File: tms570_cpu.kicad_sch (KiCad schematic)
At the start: 54 parts, among them J12 TSW-103-08-F-S-RA, J3 FTSH-105-01-L-DV-K, U2 TMS570LS0914APGEQQ1

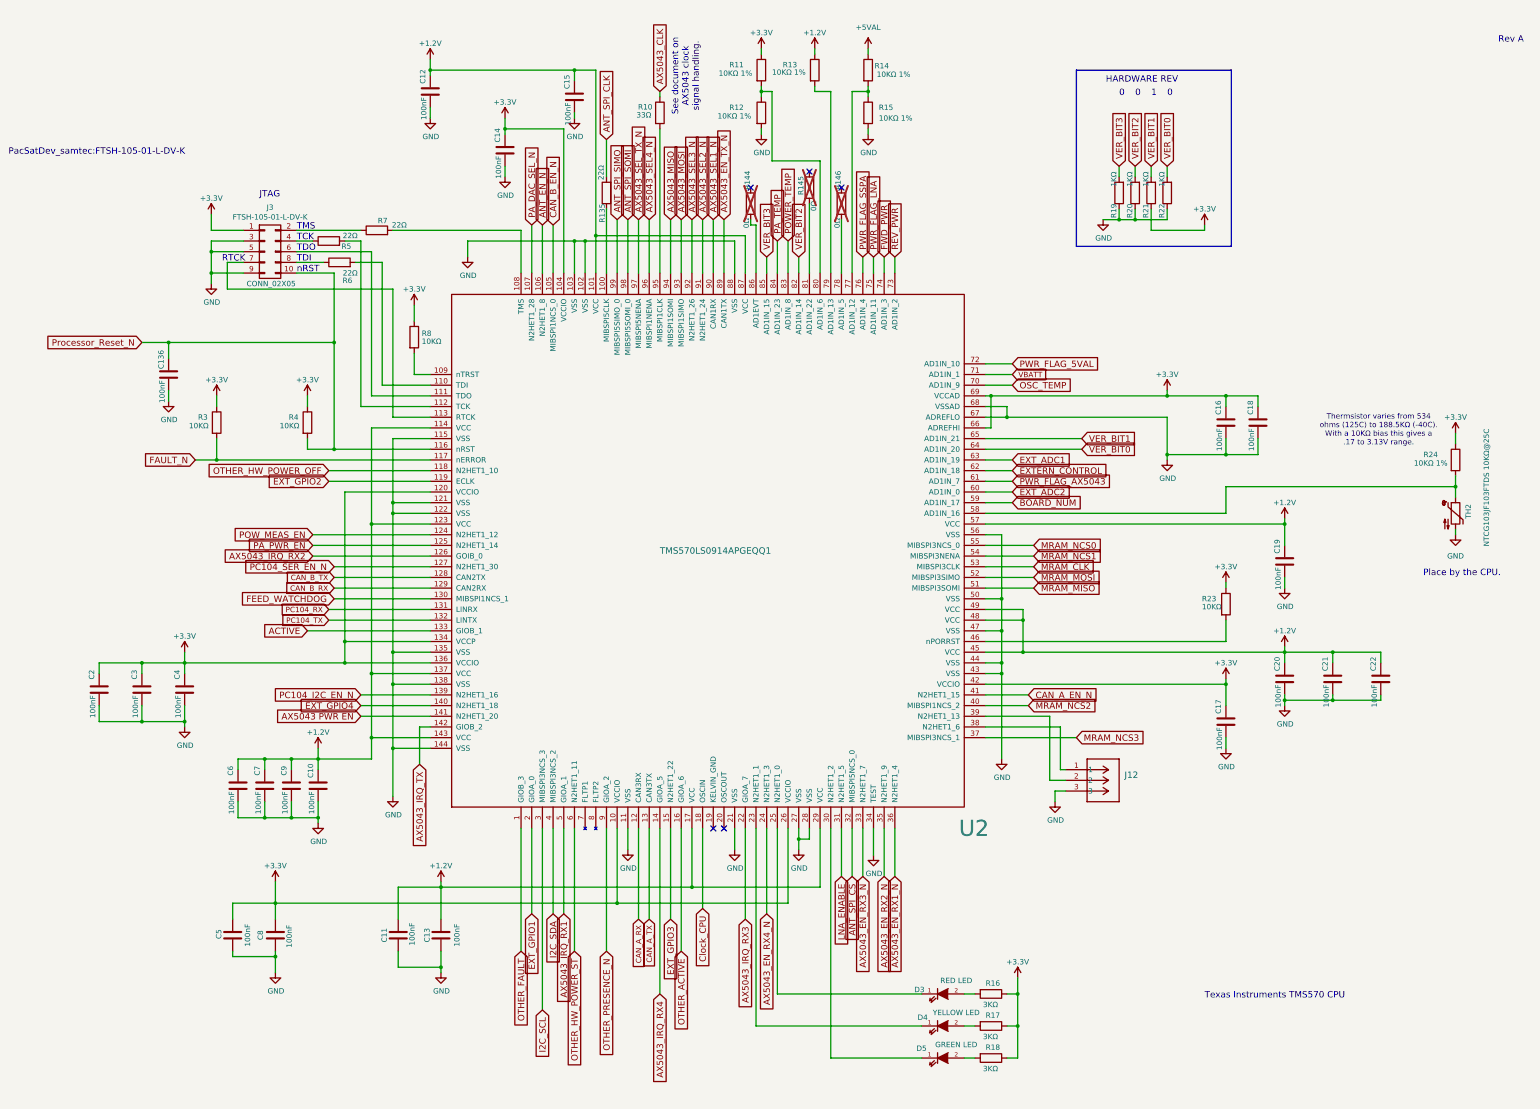
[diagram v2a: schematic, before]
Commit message: Add an interrupt line from the antenna controller to the main CPU
This required moving OTHER\_PRESENCE\_N from GIOA[2] to AD1EVT to free
up a pin with interrupts and using GIOA[2] for ANT\_IRQ\_N.

Signed-off-by: Corey Minyard <corey@minyard.net>
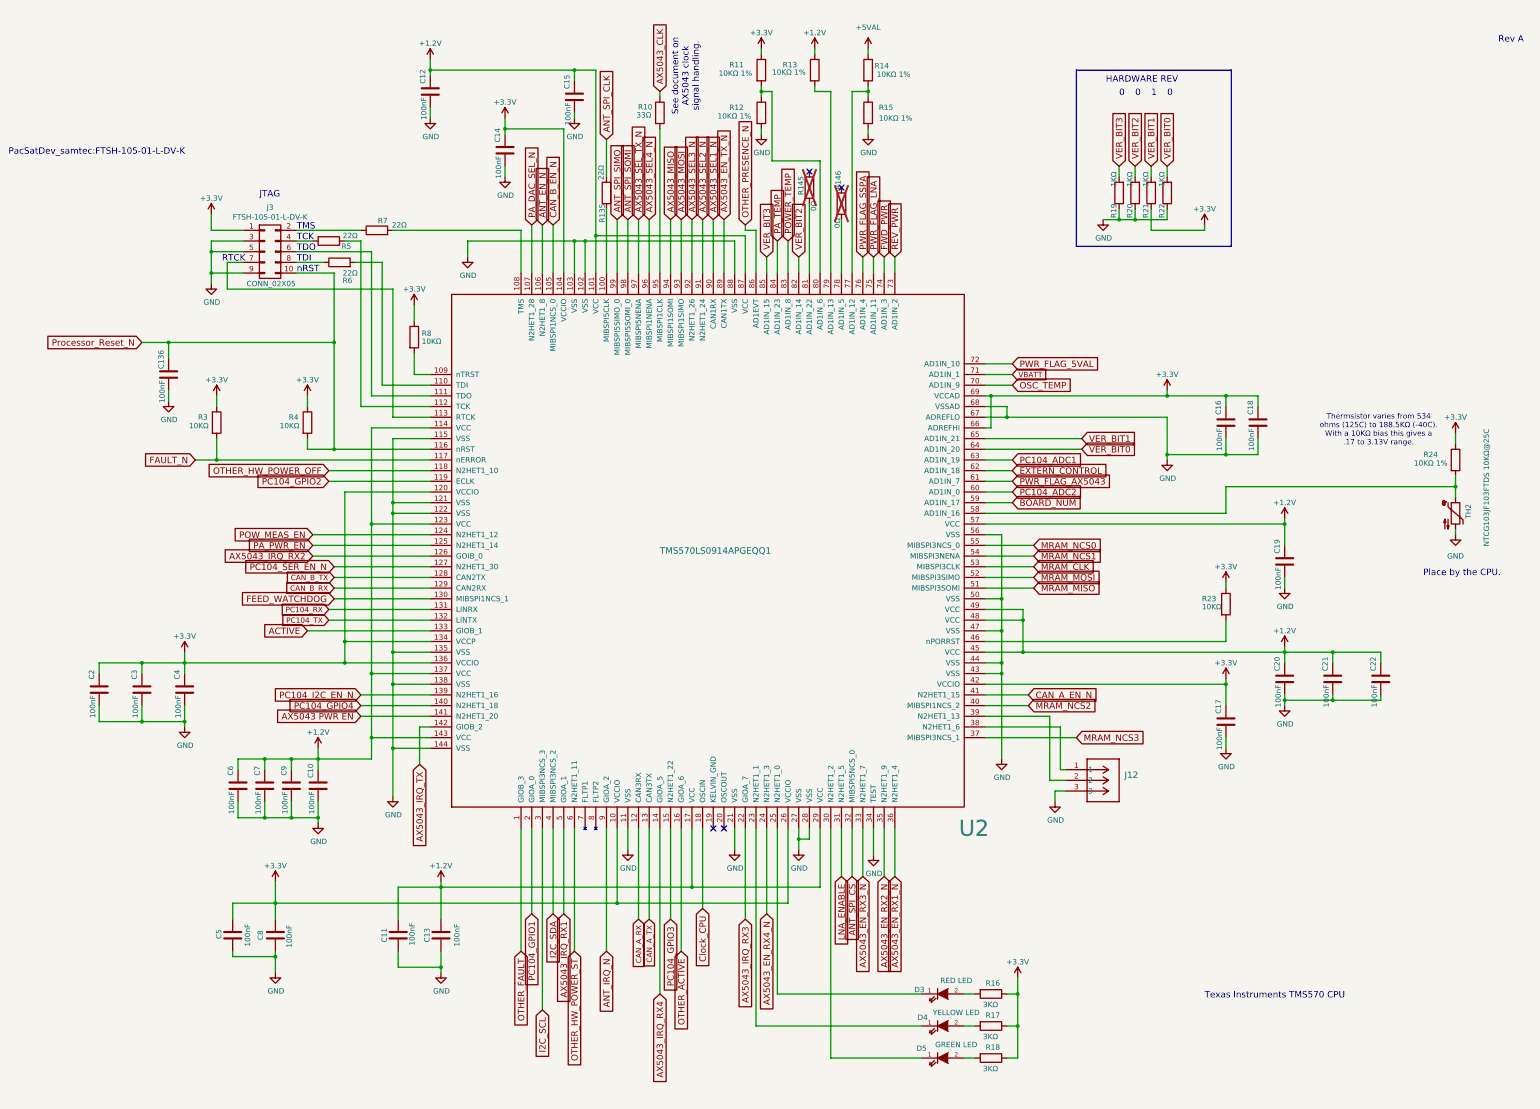
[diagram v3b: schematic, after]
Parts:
- removed R144: 0Ω, Resistor_SMD:R_0402_1005Metric_Pad0.72x0.64mm_HandSolder, symbol Device:R
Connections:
- net OTHER_PRESENCE_N: now also U2.86 (AD1EVT); no longer U2.9 (GIOA_2)
- net EXT_ADC1 renamed PC104_ADC1
- net EXT_ADC2 renamed PC104_ADC2
- net EXT_GPIO1 renamed PC104_GPIO1
- net EXT_GPIO2 renamed PC104_GPIO2
- net EXT_GPIO3 renamed PC104_GPIO3
- net EXT_GPIO4 renamed PC104_GPIO4
- new net ANT_IRQ_N: U2.9 (GIOA_2)
- no-connect marks 5 -> 4
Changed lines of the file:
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@@
 	)
 	(no_connect
-		(at 226.06 52.07)
-	)
-	(no_connect
 		(at 219.71 204.47)
 	)
@@
 	(wire
 		(pts
-			(xy 227.33 72.39) (xy 227.33 60.96)
+			(xy 224.79 62.23) (xy 224.79 60.96)
 		)
 		(stroke
@@
 	(wire
 		(pts
-			(xy 227.33 60.96) (xy 226.06 60.96)
-		)
-		(stroke
-			(width 0)
-			(type default)
-		)
-	)
-	(wire
-		(pts
 			(xy 140.97 185.42) (xy 149.86 185.42)
 		)
@@
 	(wire
 		(pts
+			(xy 227.33 62.23) (xy 227.33 72.39)
+		)
+		(stroke
+			(width 0)
+			(type default)
+		)
+	)
+	(wire
+		(pts
 			(xy 194.31 59.69) (xy 194.31 72.39)
 		)
@@
 	(wire
 		(pts
-			(xy 226.06 60.96) (xy 226.06 59.69)
-		)
-		(stroke
-			(width 0)
-			(type default)
-		)
-	)
-	(wire
-		(pts
 			(xy 254 29.21) (xy 254 30.48)
 		)
@@
 	(wire
 		(pts
+			(xy 224.79 62.23) (xy 227.33 62.23)
+		)
+		(stroke
+			(width 0)
+			(type default)
+		)
+	)
+	(wire
+		(pts
 			(xy 121.92 64.77) (xy 118.11 64.77)
 		)
@@
 		)
 	)
-	(global_label "EXT_ADC2"
+	(global_label "OTHER_HW_POWER_ST"
+		(shape input)
+		(at 184.15 233.68 270)
+		(fields_autoplaced yes)
+		(effects
+			(font
+				(size 1.524 1.524)
+			)
+			(justify right)
+		)
+		(property "Intersheetrefs" "${INTERSHEET_REFS}"
+			(at 184.15 260.9333 90)
+			(effects
+				(font
+					(size 1.27 1.27)
+				)
+				(justify right)
+				(hide yes)
+			)
+		)
+	)
+	(global_label "PC104_ADC2"
 		(shape input)
 		(at 288.29 124.46 0)
@@
 		)
 	)
-	(global_label "EXT_GPIO2"
+	(global_label "PC104_GPIO2"
 		(shape input)
 		(at 125.73 121.92 180)
@@
 		)
 	)
-	(global_label "PA_PWR_EN"
+	(global_label "ANT_IRQ_N"
 		(shape input)
-		(at 121.92 137.16 180)
+		(at 191.77 233.68 270)
 		(fields_autoplaced yes)
 		(effects
@@
 		)
 		(property "Intersheetrefs" "${INTERSHEET_REFS}"
-			(at 106.2055 137.16 0)
+			(at 191.77 248.3059 90)
 			(effects
 				(font
@@
 		)
 	)
-	(global_label "AX5043_EN_RX4_N"
+	(global_label "PA_PWR_EN"
 		(shape input)
-		(at 229.87 224.79 270)
+		(at 121.92 137.16 180)
 		(fields_autoplaced yes)
 		(effects
@@
 		)
 		(property "Intersheetrefs" "${INTERSHEET_REFS}"
-			(at 229.87 248.6323 90)
+			(at 106.2055 137.16 0)
 			(effects
 				(font
@@
 		)
 	)
-	(global_label "FAULT_N"
+	(global_label "AX5043_EN_RX4_N"
 		(shape input)
-		(at 93.98 116.84 180)
+		(at 229.87 224.79 270)
 		(fields_autoplaced yes)
 		(effects
@@
 		)
 		(property "Intersheetrefs" "${INTERSHEET_REFS}"
-			(at 81.9169 116.84 0)
+			(at 229.87 248.6323 90)
 			(effects
 				(font
@@
 		)
 	)
-	(global_label "OTHER_ACTIVE"
+	(global_label "FAULT_N"
 		(shape input)
-		(at 209.55 233.68 270)
+		(at 93.98 116.84 180)
 		(fields_autoplaced yes)
 		(effects
@@
 		)
 		(property "Intersheetrefs" "${INTERSHEET_REFS}"
-			(at 209.55 252.2974 90)
+			(at 81.9169 116.84 0)
 			(effects
 				(font
@@
 		)
 	)
-	(global_label "OTHER_PRESENCE_N"
+	(global_label "OTHER_ACTIVE"
 		(shape input)
-		(at 191.77 233.68 270)
+		(at 209.55 233.68 270)
 		(fields_autoplaced yes)
 		(effects
@@
 		)
 		(property "Intersheetrefs" "${INTERSHEET_REFS}"
-			(at 191.77 259.4095 90)
+			(at 209.55 252.2974 90)
 			(effects
 				(font
@@
 		)
 	)
-	(global_label "EXT_GPIO3"
+	(global_label "PC104_GPIO3"
 		(shape input)
 		(at 207.01 226.06 270)
@@
 		)
 	)
-	(global_label "OTHER_HW_POWER_ST"
-		(shape input)
-		(at 184.15 233.68 270)
-		(fields_autoplaced yes)
-		(effects
-			(font
-				(size 1.524 1.524)
-			)
-			(justify right)
-		)
-		(property "Intersheetrefs" "${INTERSHEET_REFS}"
-			(at 184.15 260.9333 90)
-			(effects
-				(font
-					(size 1.27 1.27)
-				)
-				(justify right)
-				(hide yes)
-			)
-		)
-	)
 	(global_label "PWR_FLAG_SSPA"
 		(shape input)
@@
 		)
 	)
-	(global_label "EXT_GPIO1"
+	(global_label "PC104_GPIO1"
 		(shape input)
 		(at 173.99 224.79 270)
@@
 		)
 	)
-	(global_label "EXT_ADC1"
+	(global_label "PC104_ADC1"
 		(shape input)
 		(at 288.29 116.84 0)
@@
 		)
 	)
-	(global_label "EXT_GPIO4"
+	(global_label "PC104_GPIO4"
 		(shape input)
 		(at 133.35 175.26 180)
@@
 		)
 	)
+	(global_label "OTHER_PRESENCE_N"
+		(shape input)
+		(at 224.79 60.96 90)
+		(fields_autoplaced yes)
+		(effects
+			(font
+				(size 1.524 1.524)
+			)
+			(justify left)
+		)
+		(property "Intersheetrefs" "${INTERSHEET_REFS}"
+			(at 224.79 35.2305 90)
+			(effects
+				(font
+					(size 1.27 1.27)
+				)
+				(justify left)
+				(hide yes)
+			)
+		)
+	)
 	(global_label "I2C_SCL"
 		(shape input)
@@
 					(unit 1)
 				)
-			)
-		)
-	)
-	(symbol
-		(lib_id "Device:R")
-		(at 226.06 55.88 0)
-		(unit 1)
-		(exclude_from_sim no)
-		(in_bom no)
-		(on_board yes)
-		(dnp yes)
-		(property "Reference" "R144"
-			(at 225.298 52.578 90)
-			(effects
-				(font
-					(size 1.27 1.27)
-				)
-				(justify left)
-			)
-		)
-		(property "Value" "0Ω"
-			(at 225.044 61.722 90)
-			(effects
-				(font
-					(size 1.27 1.27)
-				)
-				(justify left)
-			)
-		)
-		(property "Footprint" "Resistor_SMD:R_0402_1005Metric_Pad0.72x0.64mm_HandSolder"
-			(at 224.282 55.88 90)
-			(effects
-				(font
-					(size 1.27 1.27)
-				)
-				(hide yes)
-			)
-		)
-		(property "Datasheet" "~"
-			(at 226.06 55.88 0)
-			(effects
-				(font
-					(size 1.27 1.27)
-				)
-				(hide yes)
-			)
-		)
-		(property "Description" ""
-			(at 226.06 55.88 0)
-			(effects
-				(font
-					(size 1.27 1.27)
-				)
-			)
-		)
-		(pin "1"
-		)
-		(pin "2"
-		)
-		(instances
-			(project "PacSat_AFSK"
-				(path "/cc9f42d2-6985-41ac-acab-5ab7b01c5b38/adf61ae3-df77-4e04-8bda-b4049a36fcf4"
-					(reference "R144")
-					(unit 1)
-				)

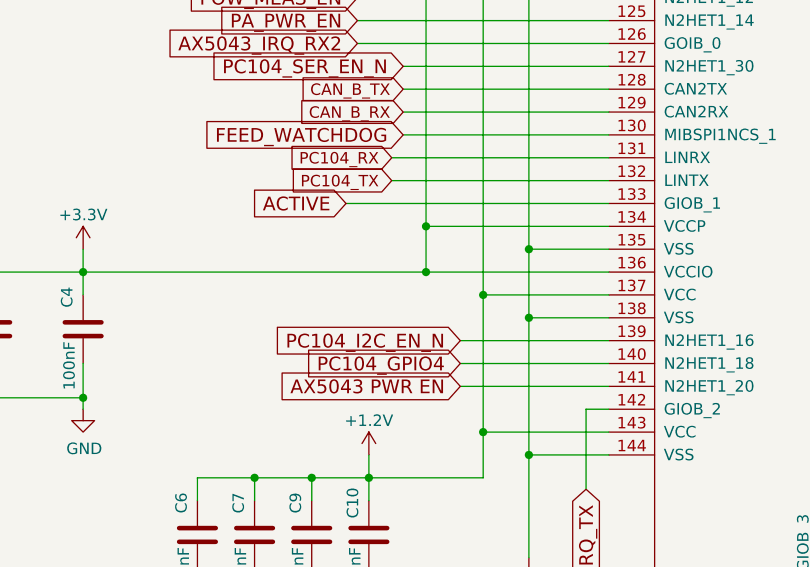
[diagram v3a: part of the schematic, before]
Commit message: Switch ACTIVE and PC104_GPIO4
ACTIVE didn't need to be interruptible, and PC104_GPIO4 might.

Signed-off-by: Corey Minyard <corey@minyard.net>
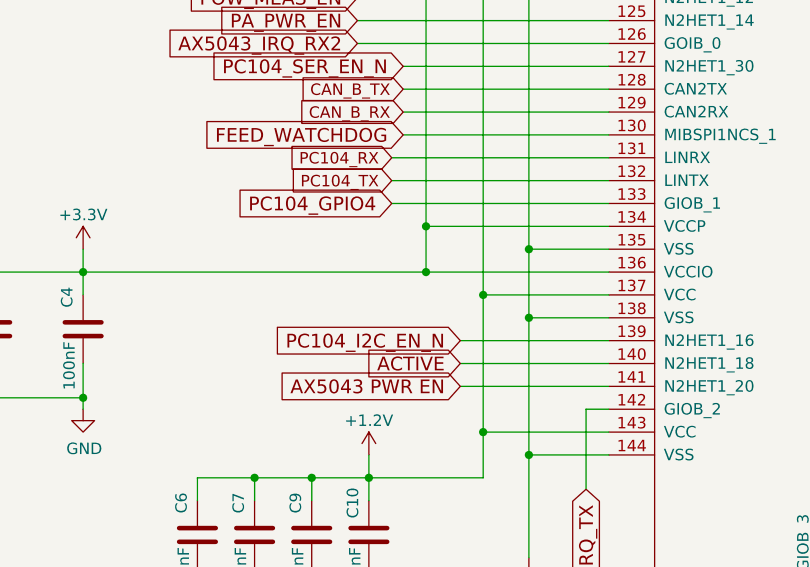
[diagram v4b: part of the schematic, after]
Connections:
- net ACTIVE: now also U2.140 (N2HET1_18); no longer U2.133 (GIOB_1)
- net PC104_GPIO4: now also U2.133 (GIOB_1); no longer U2.140 (N2HET1_18)
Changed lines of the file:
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@@
 	(wire
 		(pts
-			(xy 149.86 157.48) (xy 120.65 157.48)
+			(xy 149.86 157.48) (xy 125.73 157.48)
 		)
 		(stroke
@@
 		)
 	)
+	(global_label "ACTIVE"
+		(shape input)
+		(at 133.35 175.26 180)
+		(fields_autoplaced yes)
+		(effects
+			(font
+				(size 1.524 1.524)
+			)
+			(justify right)
+		)
+		(property "Intersheetrefs" "${INTERSHEET_REFS}"
+			(at 120.3932 175.26 0)
+			(effects
+				(font
+					(size 1.27 1.27)
+				)
+				(justify right)
+				(hide yes)
+			)
+		)
+	)
 	(global_label "POW_MEAS_EN"
 		(shape input)
@@
 		)
 	)
+	(global_label "PC104_GPIO4"
+		(shape input)
+		(at 125.73 157.48 180)
+		(fields_autoplaced yes)
+		(effects
+			(font
+				(size 1.524 1.524)
+			)
+			(justify right)
+		)
+		(property "Intersheetrefs" "${INTERSHEET_REFS}"
+			(at 110.959 157.48 0)
+			(effects
+				(font
+					(size 1.27 1.27)
+				)
+				(justify right)
+				(hide yes)
+			)
+		)
+	)
 	(global_label "PC104_SER_EN_N"
 		(shape input)
@@
 		)
 	)
-	(global_label "ACTIVE"
-		(shape input)
-		(at 120.65 157.48 180)
-		(fields_autoplaced yes)
-		(effects
-			(font
-				(size 1.524 1.524)
-			)
-			(justify right)
-		)
-		(property "Intersheetrefs" "${INTERSHEET_REFS}"
-			(at 107.6932 157.48 0)
-			(effects
-				(font
-					(size 1.27 1.27)
-				)
-				(justify right)
-				(hide yes)
-			)
-		)
-	)
 	(global_label "Clock_CPU"
 		(shape input)
@@
 				)
 				(justify right)
-				(hide yes)
-			)
-		)
-	)
-	(global_label "PC104_GPIO4"
-		(shape input)
-		(at 133.35 175.26 180)
-		(fields_autoplaced yes)
-		(effects
-			(font
-				(size 1.524 1.524)
-			)
-			(justify right)
-		)
-		(property "Intersheetrefs" "${INTERSHEET_REFS}"
-			(at 118.579 175.26 0)
-			(effects
-				(font
-					(size 1.27 1.27)
-				)
-				(justify right)

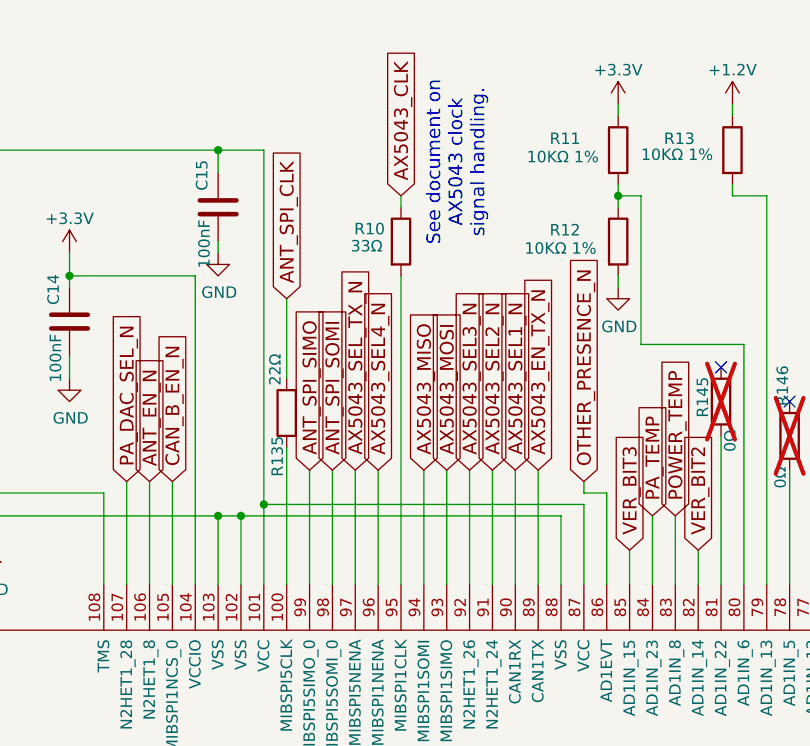
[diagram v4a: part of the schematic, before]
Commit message: Get the board ready for operation
Make the board ready as a final product, remove the lab testing portions
and add in the things required for full operation.

Signed-off-by: Corey Minyard <corey@minyard.net>
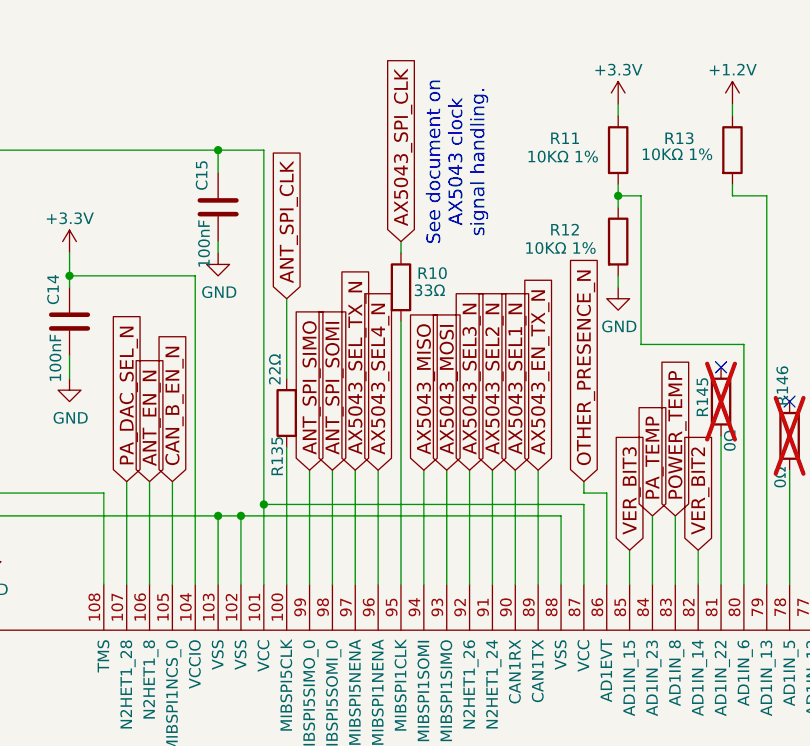
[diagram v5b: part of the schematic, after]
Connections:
- net AX5043_CLK renamed AX5043_SPI_CLK
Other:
- moved on the sheet: R10
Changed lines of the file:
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@@
 	(wire
 		(pts
-			(xy 204.47 72.39) (xy 204.47 38.1)
+			(xy 204.47 72.39) (xy 204.47 43.18)
 		)
 		(stroke
@@
 	(wire
 		(pts
-			(xy 204.47 30.48) (xy 204.47 29.21)
+			(xy 204.47 35.56) (xy 204.47 34.29)
 		)
 		(stroke
@@
 		)
 	)
-	(global_label "AX5043_CLK"
+	(global_label "AX5043_SPI_CLK"
 		(shape input)
-		(at 204.47 29.21 90)
+		(at 204.47 34.29 90)
 		(fields_autoplaced yes)
 		(effects
@@
 		)
 		(property "Intersheetrefs" "${INTERSHEET_REFS}"
-			(at 204.47 12.4071 90)
+			(at 204.47 17.4871 90)
 			(effects
 				(font
@@
 	(symbol
 		(lib_id "Device:R")
-		(at 204.47 34.29 0)
+		(at 204.47 39.37 0)
 		(unit 1)
 		(exclude_from_sim no)
@@
 		(dnp no)
 		(property "Reference" "R10"
-			(at 199.263 32.893 0)
+			(at 206.248 37.846 0)
 			(effects
 				(font
@@
 		)
 		(property "Value" "33Ω"
-			(at 198.882 34.798 0)
+			(at 205.867 39.751 0)
 			(effects
 				(font
@@
 		)
 		(property "Footprint" "Resistor_SMD:R_0402_1005Metric_Pad0.72x0.64mm_HandSolder"
-			(at 202.692 34.29 90)
+			(at 202.692 39.37 90)
 			(effects
 				(font
@@
 		)
 		(property "Datasheet" "~"
-			(at 204.47 34.29 0)
+			(at 204.47 39.37 0)
 			(effects
 				(font
@@
 		)
 		(property "Description" ""
-			(at 204.47 34.29 0)
+			(at 204.47 39.37 0)
 			(effects
 				(font
